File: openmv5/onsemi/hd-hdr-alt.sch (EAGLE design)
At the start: 58 parts, among them IC1 AP0202AT2L00XPGA0, IC2 MIC5365-2.8YC5-TR, IC3 TLV62568PDDCR, J1 DF12-36-DS, J2 DF12-36-DP, M1 9774030151R, M2 9774030151R, Q1 PMXB120EPEZ

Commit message: Add more cameras
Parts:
- removed J2: DF12-36-DP, DF12NB(3.0)-36DP-0.5V(51):DF12-36-DP
- removed L7: 100, 0402:INDUCTOR_0402
- removed M1, M2: 9774030151R, 9774030151R:9774030151R
- removed R5: 100K, rcl:R-US_R0402
- removed R6: 10K, rcl:R-US_R0402
- added C30: 22uF, SparkFun-Capacitors:22UF-0805-6.3V-20%
- added H1: LENSMOUNT20MM, lensmount:LENSMOUNT20MM
- C1, C11: value 0.22uF -> 4.7uF; device rcl:C-EUC0201 -> 0402:CAP_0402; MPN GRM033R60J224ME15D -> JMK105BBJ475MV-F
- C12: value 6.8pF -> 22uF; device 0402:CAP_0402 -> SparkFun-Capacitors:22UF-0805-6.3V-20%; MPN GRM1555C1H6R8DA01D -> CL21A226MQQNNNE
- C14, C15, C16, C19, C20: value 4.7uF -> 0.22uF; device 0402:CAP_0402 -> rcl:C-EUC0201; MPN JMK105BBJ475MV-F -> GRM033R60J224ME15D
- C17: value 22uF -> 0.22uF; device SparkFun-Capacitors:22UF-0805-6.3V-20% -> rcl:C-EUC0201; MPN CL21A226MQQNNNE -> GRM033R60J224ME15D
- C18: value 4.7uF -> 6.8pF; MPN JMK105BBJ475MV-F -> GRM1555C1H6R8DA01D
- C2: value 0.22uF -> 22uF; device rcl:C-EUC0201 -> SparkFun-Capacitors:22UF-0805-6.3V-20%; MPN GRM033R60J224ME15D -> CL21A226MQQNNNE
- C22: value 4.7uF -> 22uF; device 0402:CAP_0402 -> SparkFun-Capacitors:22UF-0805-6.3V-20%; MPN JMK105BBJ475MV-F -> CL21A226MQQNNNE
- C24, C25, C27, C28: value 22uF -> 4.7uF; device SparkFun-Capacitors:22UF-0805-6.3V-20% -> 0402:CAP_0402; MPN CL21A226MQQNNNE -> JMK105BBJ475MV-F
- IC1: value AP0202AT2L00XPGA0 -> AR0132AT6C00XPEA0; device AP0202AT2L00XPGA0:AP0202AT2L00XPGA0 -> AR0132AT6C00XPEA0:AR0132AT6C00XPEA0; MPN AP0202AT2L00XPGA0-DR -> AR0132AT6C00XPEA0-TPBR
- IC2: value MIC5365-2.8YC5-TR -> TLV62568PDDCR; device MIC5365-2.8YC5-TR:MIC5365-2.8YC5-TR -> TLV62568PDDCR:TLV62568PDDCR; MPN MIC5365-2.8YC5-TR -> TLV62568PDDCR
- IC3: value TLV62568PDDCR -> MIC5365-2.8YC5-TR; device TLV62568PDDCR:TLV62568PDDCR -> MIC5365-2.8YC5-TR:MIC5365-2.8YC5-TR; MPN TLV62568PDDCR -> MIC5365-2.8YC5-TR
- J1: value DF12-36-DS -> DF12-36-DP; device DF12-36-DS:DF12-36-DS -> DF12NB(3.0)-36DP-0.5V(51):DF12-36-DP; MPN DF12NB-36DS-0.5V(51) -> DF12NB(3.0)-36DP-0.5V(51)
- L1: value MAKK2016T2R2M -> 100; device MAKK2016T2R2M:MAKK2016T2R2M -> 0402:INDUCTOR_0402; MPN MAKK2016T2R2M -> MFBM1V1005-101-R
- L3: value 100 -> MAKK2016T2R2M; device 0402:INDUCTOR_0402 -> MAKK2016T2R2M:MAKK2016T2R2M; MPN MFBM1V1005-101-R -> MAKK2016T2R2M
- R1: value 1.5K -> 200K; MPN RC0402FR-131K5L -> CRCW0402200KFKEDC
- R2: value 1.5K -> 100K; MPN RC0402FR-131K5L -> AC0402FR-07100KL
- R3: value 100K -> 10K; MPN AC0402FR-07100KL -> AC0402FR-1310KL
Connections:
- net SENSOR_D12 renamed DCMI_D12
- net SENSOS_D13 renamed DCMI_D13
- removed net DCMI_MISO: J1.15, J2.15
- removed net DCMI_MOSI: J1.17, J2.17
- removed net DCMI_SCLK: J1.13, J2.13
- removed net DCMI_SSEL: J1.11, J2.11
- removed net SENSOR_CLK: IC1.EXT_CLK_OUT, J1.12
- removed net SENSOR_D0: IC1.DIN_0, J1.3
- removed net SENSOR_D1: IC1.DIN_1, J1.1
- removed net SENSOR_D10: IC1.DIN_10, J1.24
- removed net SENSOR_D11: IC1.DIN_11, J1.22
- removed net SENSOR_D2: IC1.DIN_2, J1.9
- removed net SENSOR_D3: IC1.DIN_3, J1.7
- removed net SENSOR_D4: IC1.DIN_4, J1.31
- removed net SENSOR_D5: IC1.DIN_5, J1.29
- removed net SENSOR_D6: IC1.DIN_6, J1.35
- removed net SENSOR_D7: IC1.DIN_7, J1.28
- removed net SENSOR_D8: IC1.DIN_8, J1.26
- removed net SENSOR_D9: IC1.DIN_9, J1.33
- removed net SENSOR_FSIN: IC1.TRIGGER_OUT/GPIO_0, J1.23
- removed net SENSOR_HSYNC: IC1.LV_IN, J1.18
- removed net SENSOR_PCLK: IC1.PIXCLK_IN, J1.14
- removed net SENSOR_RST: IC1.RESET_N_OUT, J1.21
- removed net SENSOR_SCL: IC1.M_SCLK, J1.32, R1.1
- removed net SENSOR_SDA: IC1.M_SDATA, J1.34, R2.1
- removed net SENSOR_VSYNC: IC1.FV_IN, J1.16
- removed net VDDIO_H: C13.2, C19.2, C2.2, C25.2, C3.2, C4.2, IC1.EXT_REG, IC1.SADDR, IC1.VDDIO_H0, IC1.VDDIO_H1, IC1.VDDIO_H2, IC1.VDD_REG, L3.P$1
- removed net VDDIO_OTPM: C10.2, C18.2, C24.2, IC1.VDDIO_OTPM, L2.P$1
- removed net VDDIO_S: C1.2, C20.2, C26.2, IC1.VDDIO_S, L4.P$1
- removed net VDD_PHY: C11.2, C21.2, C27.2, IC1.VDD_PHY, L5.P$1
- new net DCMI_D10: IC1.DOUT10, J1.24
- new net DCMI_D11: IC1.DOUT11, J1.22
- new net DCMI_D8: IC1.DOUT8, J1.26
- new net DCMI_D9: IC1.DOUT9, J1.33
- new net SPI_MISO: J1.15
- new net SPI_MOSI: J1.17
- new net SPI_SCLK: J1.13
- new net SPI_SSEL: J1.11
- new net VAA: C25.2, C26.2, C4.1, C5.1, IC1.VAA0, IC1.VAA1, L4.P$1
- new net VAA_PIX: C13.1, C14.1, C27.2, C29.2, IC1.VAA_PIX0, IC1.VAA_PIX1, L5.P$1
- new net VDDIO: C15.1, C16.1, C17.1, C19.1, C20.1, C28.2, C30.2, IC1.VDDIO0, IC1.VDDIO1, IC1.VDDIO2, IC1.VDDIO3, IC1.VDDIO4, L6.P$1
- net DCMI_CLK: now also J1.12; no longer J2.12
- net DCMI_D0: now also IC1.DOUT0, J1.3; no longer IC1.DOUT_16, J2.31
- net DCMI_D1: now also IC1.DOUT1, J1.1; no longer IC1.DOUT_17, J2.29
- net DCMI_D2: now also IC1.DOUT2, J1.9; no longer IC1.DOUT_18, J2.35
- net DCMI_D3: now also IC1.DOUT3, J1.7; no longer IC1.DOUT_19, J2.28
- net DCMI_D4: now also IC1.DOUT4, J1.31; no longer IC1.DOUT_20, J2.26
- net DCMI_D5: now also IC1.DOUT5, J1.29; no longer IC1.DOUT_21, J2.33
- net DCMI_D6: now also IC1.DOUT6, J1.35; no longer IC1.DOUT_22, J2.24
- net DCMI_D7: now also IC1.DOUT7, J1.28; no longer IC1.DOUT_23, J2.22
- net DCMI_FSIN: now also IC1.TRIGGER, J1.23; no longer IC1.FRAME_SYNC, J2.23
- net DCMI_HSYNC: now also IC1.LINE_VALID, J1.18; no longer IC1.LV_OUT, J2.18
- net DCMI_PCLK: now also IC1.PIXCLK, J1.14; no longer IC1.PIXCLK_OUT, J2.14
- net DCMI_PWDN: no longer IC1.STANDBY, J2.25
- net DCMI_PWDN_INT: now also IC3.EN, R4.1; no longer IC2.EN, R5.1
- net DCMI_RST: now also J1.21, R3.2; no longer J2.21, R6.2
- net DCMI_SCL: now also J1.32; no longer J2.32
- net DCMI_SDA: now also J1.34; no longer J2.34
- net DCMI_VSYNC: now also IC1.FRAME_VALID, J1.16; no longer IC1.FV_OUT, J2.16
- net FB: now also C18.2, IC2.FB, R1.1, R2.1; no longer C12.2, IC3.FB, R3.1, R4.1
- net GND: now also C10.2, C12.1, C13.2, C14.2, C15.2, C16.2, C17.2, C19.2, C20.2, C3.2, C30.1, C4.2, C5.2, C6.2, C7.2, C8.2, C9.2, IC1.AGND0, IC1.AGND1, IC1.DGND0, IC1.DGND1, IC1.DGND2, IC1.DGND3, IC1.DGND4, IC1.DGND5, IC1.DGND6, IC1.OE_N, IC1.SADDR, IC1.STANDBY, R2.2; no longer C10.1, C13.1, C14.1, C15.1, C16.1, C17.1, C18.1, C19.1, C20.1, C3.1, C4.1, C5.1, C6.1, C7.1, C8.1, C9.1, IC1.DGND, IC1.ENDLO, IC1.GND0, IC1.GND1, IC1.GND2, IC1.GND3, IC1.GND4, IC1.GND5, IC1.GND6, IC1.GND7, IC1.HISPI0N, IC1.HISPI0P, IC1.HISPI1N, IC1.HISPI1P, IC1.HISPICN, IC1.HISPICP, IC1.RESERVED_0, IC1.RESERVED_1, IC1.SPI_SDI, J2.19, J2.27, J2.5, R5.2
- net RESET_N: now also IC2.PG, R3.1; no longer IC3.PG, R6.1
- net SW: now also IC2.SW, L3.2; no longer IC3.SW, L1.2
- net VCC: now also C21.2; no longer C15.2, C16.2, IC3.VIN, J2.10, J2.2, J2.20, J2.30, J2.36, L2.P$2, L3.P$2, Q1.S, R1.2, R2.2
- net VDD: now also C1.2, C10.1, C2.2, C6.1, C7.1, C8.1, C9.1, IC1.VDD4, L1.P$1; no longer C23.2, C29.2, C6.2, C7.2, C8.2, C9.2, L7.P$1
- net VDDA: now also C24.2, IC3.VIN, Q1.S; no longer J2.4
- net VDDIO_REG: now also C23.2, IC2.EN, IC3.VOUT, L2.P$2, L6.P$2; no longer C14.2, IC2.VOUT, IC3.EN
- net VDD_PLL: now also C11.2, C12.2, C3.1, L2.P$1; no longer C22.2, C28.2, C5.2, L6.P$1
- net VDD_REG: now also C18.1, C22.2, L1.P$2, L3.1, R1.2; no longer C12.1, C17.2, L1.1, L6.P$2, L7.P$2, R3.2
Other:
- note added: "1.8V"
- note added: "Camera Sensor"
- note added: "Connector"
- note removed: "1.2V"
- note removed: "Host Connector"
- note removed: "ISP"
- note removed: "SENSOR CONNECTOR"
- moved on the sheet: C1, C10, C11, C12, C13, C14, C15, C16, C17, C18, C19, C2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

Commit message: Finish out new onsemi cameras
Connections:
- removed net DCMI_D12: J1.8
- removed net DCMI_D13: J1.6
- net GND: now also J1.6, J1.8
- net SPI_MISO: now also IC1.FLASH
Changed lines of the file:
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@@
 <wire x1="17.78" y1="215.9" x2="43.18" y2="215.9" width="0.1524" layer="91"/>
+</segment>
+<segment>
+<wire x1="381" y1="228.6" x2="411.48" y2="228.6" width="0.1524" layer="91"/>
+<label x="386.08" y="228.6" size="1.778" layer="95"/>
+<pinref part="J1" gate="G$1" pin="6"/>
+</segment>
+<segment>
+<wire x1="381" y1="226.06" x2="411.48" y2="226.06" width="0.1524" layer="91"/>
+<label x="386.08" y="226.06" size="1.778" layer="95"/>
+<pinref part="J1" gate="G$1" pin="8"/>
 </segment>
 </net>
@@
 <pinref part="J1" gate="G$1" pin="15"/>
 </segment>
+<segment>
+<pinref part="IC1" gate="G$1" pin="FLASH"/>
+<wire x1="43.18" y1="187.96" x2="22.86" y2="187.96" width="0.1524" layer="91"/>
+<label x="25.4" y="187.96" size="1.778" layer="95"/>
+</segment>
 </net>
 <net name="SPI_MOSI" class="4">
@@
 </segment>
 </net>
-<net name="DCMI_D13" class="4">
-<segment>
-<wire x1="381" y1="228.6" x2="411.48" y2="228.6" width="0.1524" layer="91"/>
-<label x="386.08" y="228.6" size="1.778" layer="95"/>
-<pinref part="J1" gate="G$1" pin="6"/>
-</segment>
-</net>
-<net name="DCMI_D12" class="4">
-<segment>
-<wire x1="381" y1="226.06" x2="411.48" y2="226.06" width="0.1524" layer="91"/>
-<label x="386.08" y="226.06" size="1.778" layer="95"/>
-<pinref part="J1" gate="G$1" pin="8"/>
-</segment>
-</net>

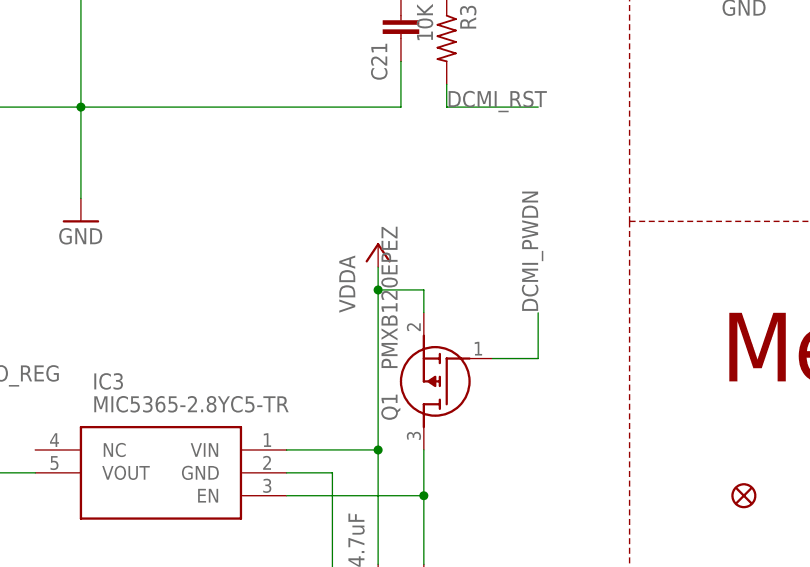
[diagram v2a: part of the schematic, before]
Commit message: Update camera modules to use different non-flippable pmosfet
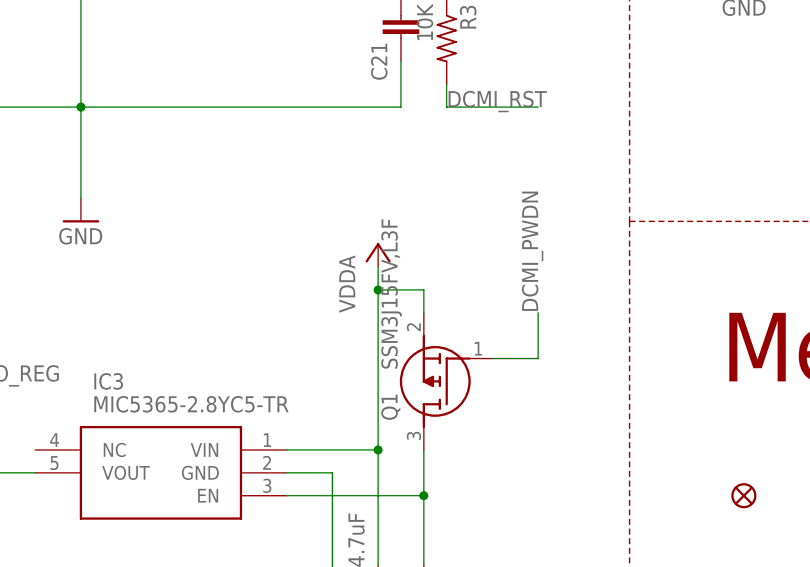
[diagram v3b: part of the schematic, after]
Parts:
- Q1: value PMXB120EPEZ -> SSM3J15FV,L3F; device PMXB120EPEZ:PMXB120EPEZ -> SSM3J15FV_L3F:SSM3J15FV,L3F; MPN PMXB120EPEZ -> SSM3J15FV,L3F
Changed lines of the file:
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@@
 </part>
 <part name="GND11" library="supply" deviceset="GND" device=""/>
-<part name="Q1" library="PMXB120EPEZ" deviceset="PMXB120EPEZ" device="">
-<attribute name="MPN" value="PMXB120EPEZ"/>
+<part name="Q1" library="SSM3J15FV_L3F" deviceset="SSM3J15FV,L3F" device="">
+<attribute name="MPN" value="SSM3J15FV,L3F"/>
 </part>
 <part name="R4" library="rcl" library_urn="urn:adsk.eagle:library:334" deviceset="R-US_" device="R0402" package3d_urn="urn:adsk.eagle:package:23547/3" value="100K">
